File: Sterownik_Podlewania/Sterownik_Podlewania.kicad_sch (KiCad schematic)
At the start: 29 parts, among them J18 RJ45, J3 RJ45, J4 Conn_01x04_Socket, J5 RJ45, J6 RJ45, J8 RJ45, U1 ESP32-DEVKITC, U5 757

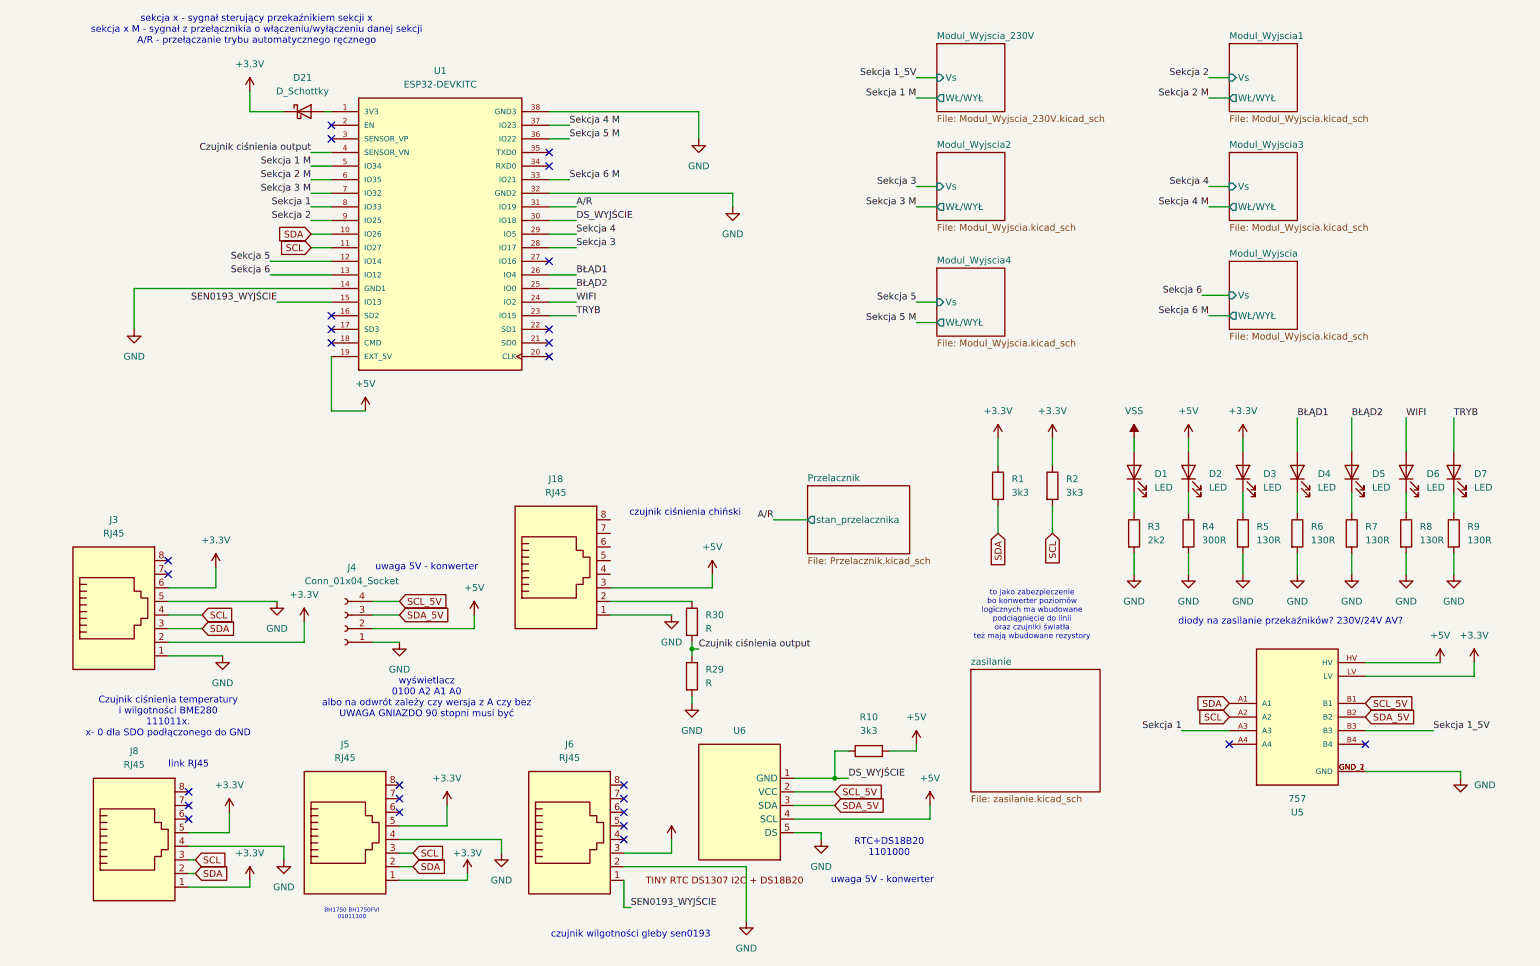
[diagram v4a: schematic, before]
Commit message: Zmiana footprintó diód przekaźnika na schottky,finalne ułożenie  przekaźników, diód itp
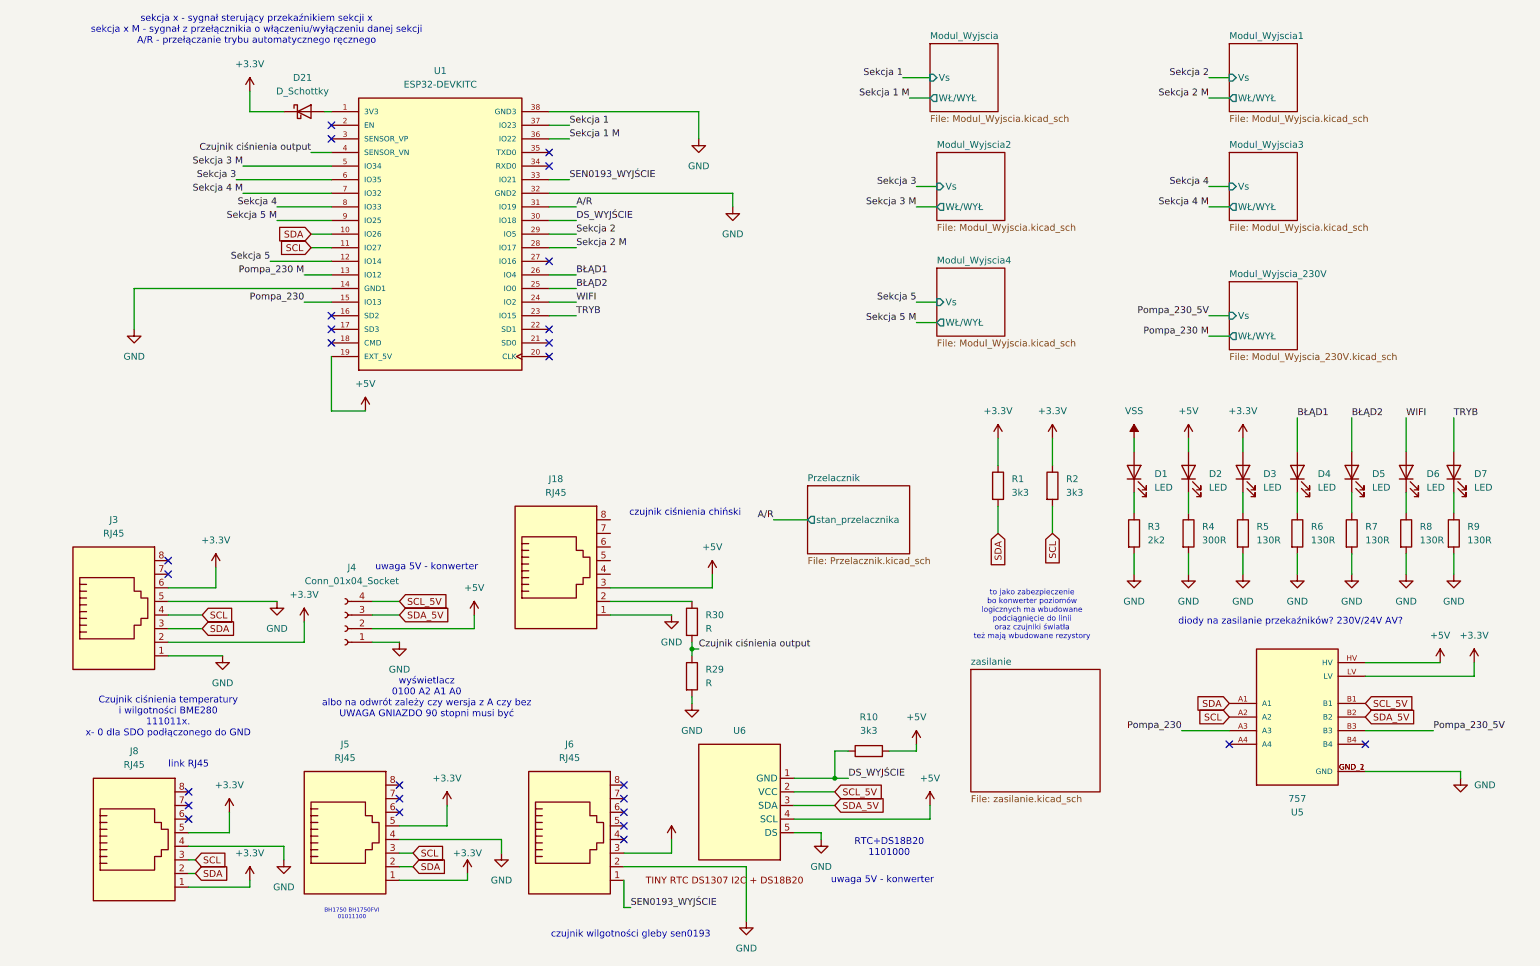
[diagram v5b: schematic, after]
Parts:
- D21: footprint Diode_SMD:D_SOD-123 -> Diode_SMD:D_1206_3216Metric
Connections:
- net Sekcja 6 M is gone; now on net SEN0193_WYJŚCIE: U1.33 (IO21)
- net SEN0193_WYJŚCIE: no longer U1.15 (IO13)
- net Sekcja 1: now also U1.37 (IO23); no longer U1.8 (IO33), U5.A3
- net Sekcja 1 M: now also U1.36 (IO22); no longer U1.5 (IO34)
- net Sekcja 2: now also U1.29 (IO5); no longer U1.9 (IO25)
- net Sekcja 2 M: now also U1.28 (IO17); no longer U1.6 (IO35)
- net Sekcja 3: now also U1.6 (IO35); no longer U1.28 (IO17)
- net Sekcja 3 M: now also U1.5 (IO34); no longer U1.7 (IO32)
- net Sekcja 4: now also U1.8 (IO33); no longer U1.29 (IO5)
- net Sekcja 4 M: now also U1.7 (IO32); no longer U1.37 (IO23)
- net Sekcja 5 M: now also U1.9 (IO25); no longer U1.36 (IO22)
- net Sekcja 1_5V renamed Pompa_230_5V
- net Sekcja 6 renamed Pompa_230 M
- new net Pompa_230: U1.15 (IO13), U5.A3
